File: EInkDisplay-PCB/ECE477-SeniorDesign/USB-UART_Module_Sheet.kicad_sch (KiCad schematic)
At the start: 6 parts, among them J2 USB_B, U1 CP2102-GMR

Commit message: push
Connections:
- net USART1_RX: now also U1.25 (RXD); no longer U1.26 (TXD)
- net USART1_TX: now also U1.26 (TXD); no longer U1.25 (RXD)
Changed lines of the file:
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@@
-		)
-	)
-	(global_label "USART1_TX"
-		(shape input)
-		(at 167.64 69.85 0)
-		(fields_autoplaced yes)
-		(effects
-			(font
-				(size 1.27 1.27)
-			)
-			(justify left)
-		)
-		(property "Intersheetrefs" "${INTERSHEET_REFS}"
-			(at 180.8456 69.85 0)
-			(effects
-				(font
-					(size 1.27 1.27)
-				)
-				(justify left)
-				(hide yes)
-			)
-		)
-	)
-	(global_label "USART1_RX"
-		(shape input)
-		(at 167.64 67.31 0)
-		(fields_autoplaced yes)
-		(effects
-			(font
-				(size 1.27 1.27)
-			)
-			(justify left)
-		)
-		(property "Intersheetrefs" "${INTERSHEET_REFS}"
-			(at 181.148 67.31 0)
-			(effects
-				(font
-					(size 1.27 1.27)
-				)
-				(justify left)
-				(hide yes)
-			)
 		)
 	)
@@
 		)
 	)
+	(hierarchical_label "USART1_RX"
+		(shape input)
+		(at 167.64 69.85 0)
+		(effects
+			(font
+				(size 1.27 1.27)
+			)
+			(justify left)
+		)
+	)
+	(hierarchical_label "USART1_TX"
+		(shape input)
+		(at 167.64 67.31 0)
+		(effects
+			(font
+				(size 1.27 1.27)
+			)
+			(justify left)
+		)
+	)

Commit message: push
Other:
- note added: "Going to have to consider diff pairs when designing PCB"
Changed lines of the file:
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@@
+		)
+	)
+	(text "Going to have to consider diff pairs when designing PCB\n"
+		(exclude_from_sim no)
+		(at 110.998 62.738 0)
+		(effects
+			(font
+				(size 1.27 1.27)
+			)
 		)
 	)

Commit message: push
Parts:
- added TP14: VBUS, symbol Connector:TestPoint
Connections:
- net VBUS: now also TP14.1
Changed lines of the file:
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@@
+	)
+	(junction
+		(at 119.38 85.09)
+		(diameter 0)
+		(color 0 0 0 0)
 	)
 	(junction
@@
 	(wire
 		(pts
+			(xy 119.38 85.09) (xy 119.38 90.17)
+		)
+		(stroke
+			(width 0)
+			(type default)
+		)
+	)
+	(wire
+		(pts
 			(xy 153.67 71.12) (xy 153.67 74.93)
 		)
@@
 	(wire
 		(pts
-			(xy 119.38 85.09) (xy 119.38 90.17)
+			(xy 119.38 78.74) (xy 119.38 85.09)
 		)
 		(stroke
@@
 	(global_label "VBUS"
 		(shape input)
-		(at 119.38 85.09 90)
+		(at 119.38 78.74 90)
 		(fields_autoplaced yes)
 		(effects
@@
 		)
 		(property "Intersheetrefs" "${INTERSHEET_REFS}"
-			(at 119.38 77.2062 90)
+			(at 119.38 70.8562 90)
 			(effects
 				(font
@@
 		)
 	)
+	(symbol
+		(lib_id "Connector:TestPoint")
+		(at 119.38 85.09 90)
+		(unit 1)
+		(exclude_from_sim no)
+		(in_bom yes)
+		(on_board yes)
+		(dnp no)
+		(fields_autoplaced yes)
+		(property "Reference" "TP14"
+			(at 116.078 80.01 90)
+			(effects
+				(font
+					(size 1.27 1.27)
+				)
+			)
+		)
+		(property "Value" "VBUS"
+			(at 116.078 82.55 90)
+			(effects
+				(font
+					(size 1.27 1.27)
+				)
+			)
+		)
+		(property "Footprint" ""
+			(at 119.38 80.01 0)
+			(effects
+				(font
+					(size 1.27 1.27)
+				)
+				(hide yes)
+			)
+		)
+		(property "Datasheet" "~"
+			(at 119.38 80.01 0)
+			(effects
+				(font
+					(size 1.27 1.27)
+				)
+				(hide yes)
+			)
+		)
+		(property "Description" "test point"
+			(at 119.38 85.09 0)
+			(effects
+				(font
+					(size 1.27 1.27)
+				)
+				(hide yes)
+			)
+		)
+		(pin "1"
+		)
+		(instances
+			(project ""
+				(path "/527ae649-08be-4368-9cf9-441ebba18eca/b5fe9c37-5cbb-4476-b922-2ef94ca58b1e"
+					(reference "TP14")
+					(unit 1)
+				)
+			)
+		)
+	)

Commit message: fixing things
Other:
- moved on the sheet: TP14
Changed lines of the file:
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@@
-	)
-	(junction
-		(at 119.38 85.09)
-		(diameter 0)
-		(color 0 0 0 0)
 	)
 	(junction
@@
 	)
 	(junction
+		(at 119.38 78.74)
+		(diameter 0)
+		(color 0 0 0 0)
+	)
+	(junction
 		(at 119.38 90.17)
 		(diameter 0)
@@
 	(wire
 		(pts
-			(xy 119.38 85.09) (xy 119.38 90.17)
-		)
-		(stroke
-			(width 0)
-			(type default)
-		)
-	)
-	(wire
-		(pts
 			(xy 153.67 71.12) (xy 153.67 74.93)
 		)
@@
 	(wire
 		(pts
+			(xy 119.38 78.74) (xy 119.38 90.17)
+		)
+		(stroke
+			(width 0)
+			(type default)
+		)
+	)
+	(wire
+		(pts
 			(xy 124.46 87.63) (xy 133.35 87.63)
 		)
@@
 	(wire
 		(pts
-			(xy 119.38 78.74) (xy 119.38 85.09)
+			(xy 119.38 71.12) (xy 119.38 78.74)
 		)
 		(stroke
@@
 	(wire
 		(pts
-			(xy 119.38 90.17) (xy 111.76 90.17)
+			(xy 111.76 90.17) (xy 119.38 90.17)
 		)
 		(stroke
@@
 	(global_label "VBUS"
 		(shape input)
-		(at 119.38 78.74 90)
+		(at 119.38 71.12 90)
 		(fields_autoplaced yes)
 		(effects
@@
 		)
 		(property "Intersheetrefs" "${INTERSHEET_REFS}"
-			(at 119.38 70.8562 90)
+			(at 119.38 63.2362 90)
 			(effects
 				(font
@@
 	(symbol
 		(lib_id "Connector:TestPoint")
-		(at 119.38 85.09 90)
+		(at 119.38 78.74 90)
 		(unit 1)
 		(exclude_from_sim no)
@@
 		(fields_autoplaced yes)
 		(property "Reference" "TP14"
-			(at 116.078 80.01 90)
+			(at 116.078 73.66 90)
 			(effects
 				(font
@@
 		)
 		(property "Value" "VBUS"
-			(at 116.078 82.55 90)
+			(at 116.078 76.2 90)
 			(effects
 				(font
@@
 		)
 		(property "Footprint" ""
-			(at 119.38 80.01 0)
+			(at 119.38 73.66 0)
 			(effects
 				(font
@@
 		)
 		(property "Datasheet" "~"
-			(at 119.38 80.01 0)
+			(at 119.38 73.66 0)
 			(effects
 				(font
@@
 		)
 		(property "Description" "test point"
-			(at 119.38 85.09 0)
-			(effects
-				(font
+			(at 119.38 78.74 0)
+			(effects
+				(font

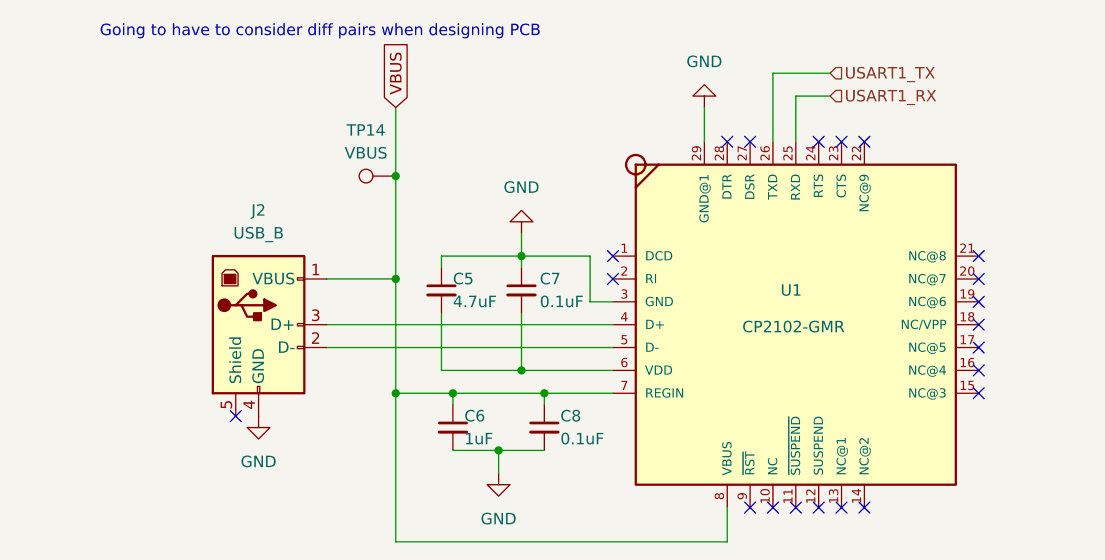
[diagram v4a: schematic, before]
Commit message: Update USB-UART_Module_Sheet.kicad_sch
Add ESD diode
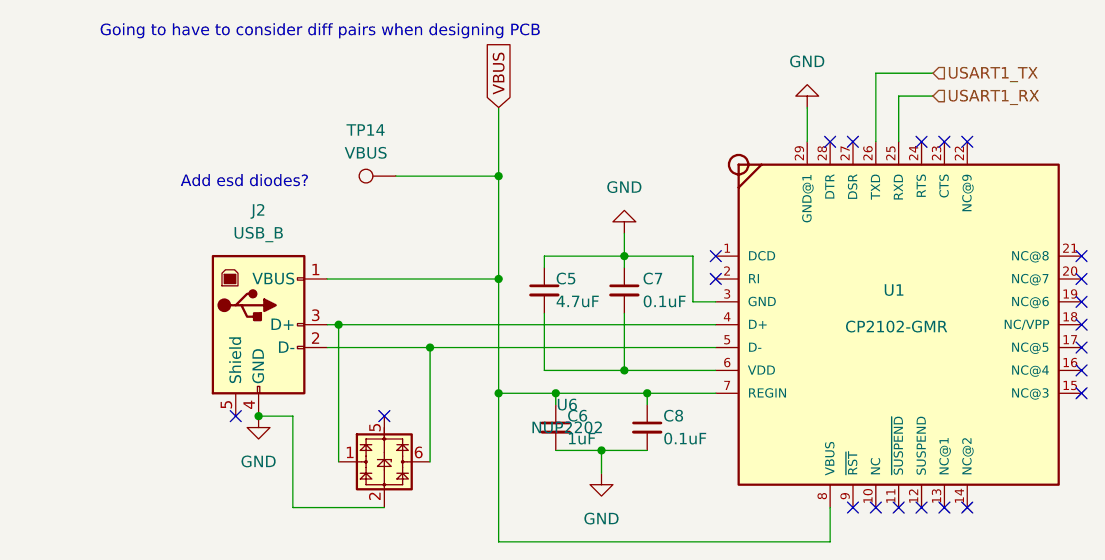
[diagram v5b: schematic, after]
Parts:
- added U6: NUP2202, Package_TO_SOT_SMD:SOT-363_SC-70-6, symbol Power_Protection:NUP2202
- C5, C6, C7, C8: footprint (none) -> Capacitor_SMD:C_0805_2012Metric_Pad1.18x1.45mm_HandSolder
- J2: footprint (none) -> Connector_USB:USB_B_TE_5787834_Vertical
- U1: footprint INTERFACE-CP2102-GMR_QFN28_:QFN28G_0.5-5X5MM -> CP2102-GMR:QFN28_5X5_SIL
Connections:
- net GND: now also U6.2
- net at J2.3 (D+), U1.4 (D+): now also U6.1
- net at J2.2 (D-), U1.5 (D-): now also U6.6
- no-connect marks 21 -> 22
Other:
- note added: "Add esd diodes?"
- moved on the sheet: C5, C6, C7, C8, U1
